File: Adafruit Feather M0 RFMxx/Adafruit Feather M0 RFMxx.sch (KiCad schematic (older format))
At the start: 39 parts, among them SW1 SPST_TACT-KMR2, U2 AP2112K-3.3, U3 MCP73831T-2ACI/OT, U4 RFM69HCW, X1 JSTPH, X2 32.768, X3 microUSB, X4 uFL

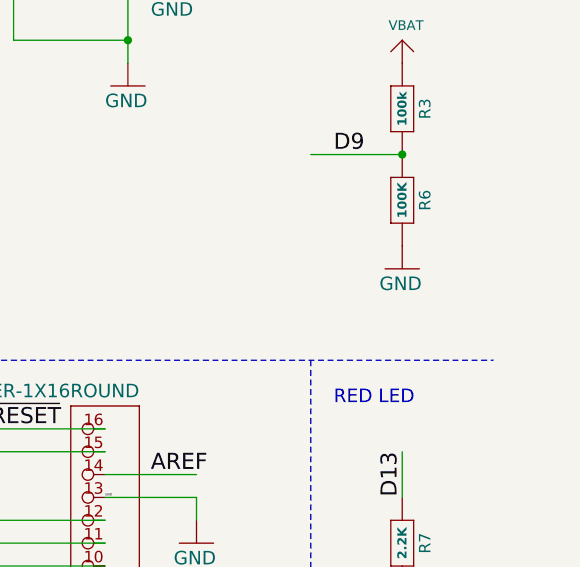
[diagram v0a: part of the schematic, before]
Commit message: Found cause of GND airwire around 144,100: ground pour on bottom was interrupted by routing of i2c to qwiic connector.  Moving it to allow GND to connect eliminated issue.
Still have complaint about TOP and BOTTOM GND pours not connected.
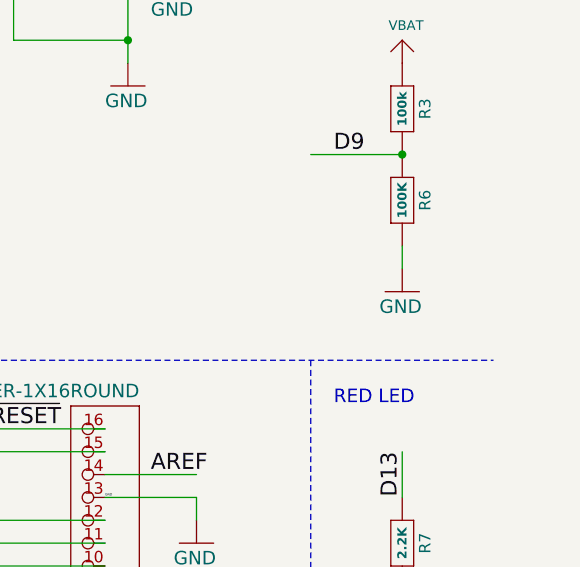
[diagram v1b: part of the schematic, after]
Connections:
- wire segments 160 -> 161
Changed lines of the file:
@@
 L Adafruit_Feather_M0_RFMxx-eagle-import:GND #GND013
 U 1 0 1DDAFC179E3D6951
-P 13600 3700
-F 0 "#GND013" H 13600 3700 50  0001 C CNN
-F 1 "GND" H 13500 3600 59  0000 L BNN
-F 2 "" H 13600 3700 50  0001 C CNN
-F 3 "" H 13600 3700 50  0001 C CNN
-	1    13600 3700
+P 13600 3800
+F 0 "#GND013" H 13600 3800 50  0001 C CNN
+F 1 "GND" H 13500 3700 59  0000 L BNN
+F 2 "" H 13600 3800 50  0001 C CNN
+F 3 "" H 13600 3800 50  0001 C CNN
+	1    13600 3800
 	1    0    0    -1
 $EndComp
@@
 Text Label 2300 1600 0    50   ~ 0
 SCL
+Wire Wire Line
+	13600 3600 13600 3700
 $EndSCHEMATC
